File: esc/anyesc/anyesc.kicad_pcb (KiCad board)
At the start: 4 copper layers, 42.2 x 17.8 mm, 46 parts, among them J1 USB_C_Receptacle_USB2.0, J2 Conn_01x04, J3 5530843-7, SW1 SW_Push, SW2 SW_Push, U1 RP2040, U2 W25Q64JVXGIQ, U3 B-G431B-ESC1, Y1 12MHz

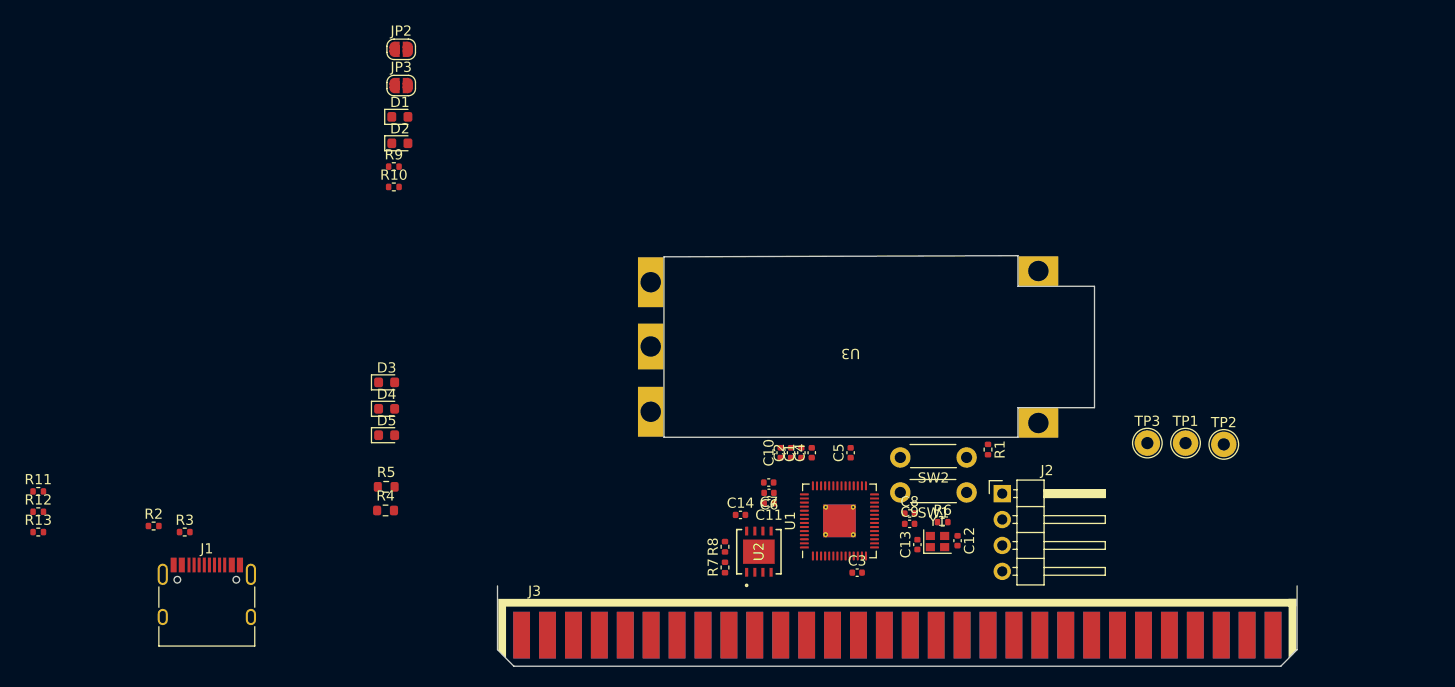
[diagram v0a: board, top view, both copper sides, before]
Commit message: Feat[anyesc]: initial anyesc pcb design
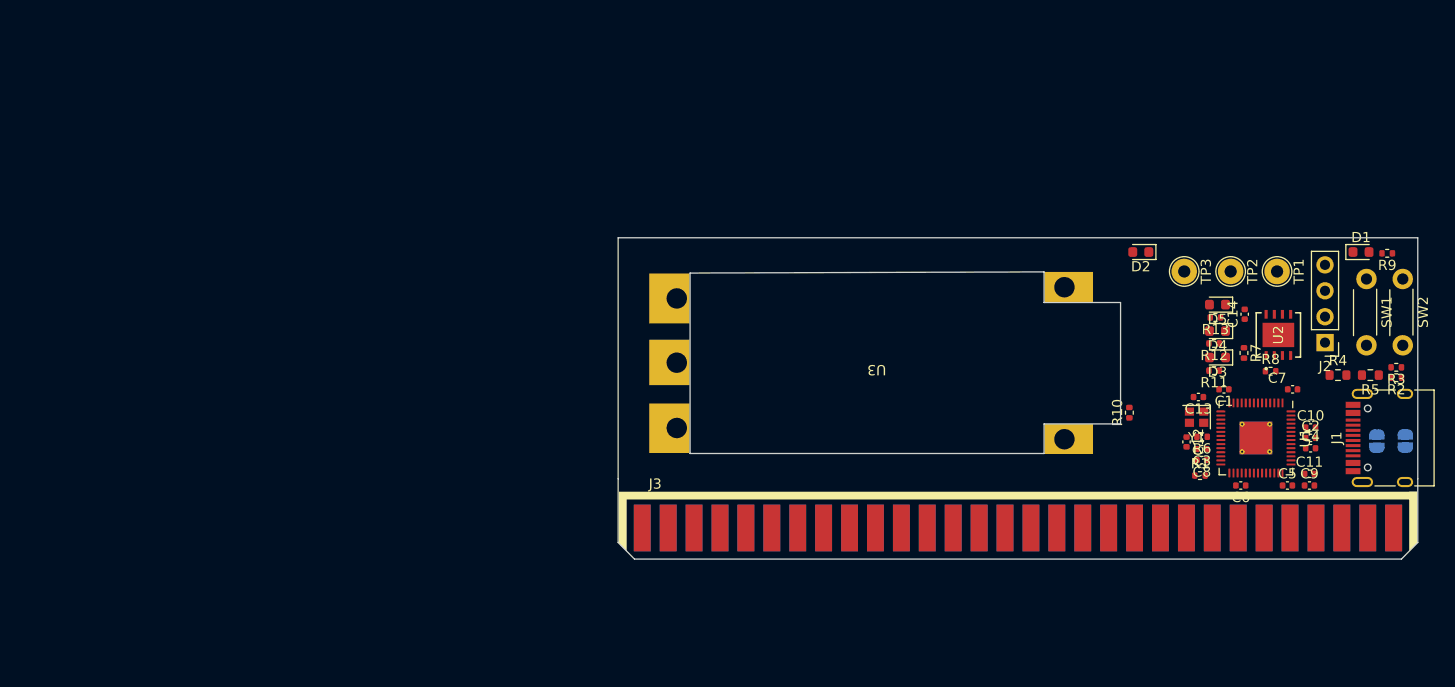
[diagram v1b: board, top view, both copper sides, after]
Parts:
- J2: footprint Connector_PinHeader_2.54mm:PinHeader_1x04_P2.54mm_Horizontal -> Connector_PinHeader_2.54mm:PinHeader_1x04_P2.54mm_Vertical
- JP2, JP3: moved to B.Cu
- moved R2 122.7 mm to (184.0, 105.2), turned to 180 degrees
- moved R3 119.9 mm to (184.0, 104.2), turned to 180 degrees
- moved J1 117.6 mm to (183.8, 111.1), turned to 90 degrees
- moved R13 117.3 mm to (166.3, 99.3), turned to 180 degrees
- moved R12 116.4 mm to (166.2, 101.9), turned to 180 degrees
- moved R11 115.9 mm to (166.2, 104.5), turned to 180 degrees
- moved JP3 104.4 mm to (184.9, 111.4), turned to -90 degrees
- moved JP2 103.1 mm to (182.1, 111.4), turned to -90 degrees
- moved R9 97.7 mm to (183.2, 93.0), turned to 180 degrees
- moved R5 97.1 mm to (181.5, 105.0), turned to 180 degrees
- moved D1 95.1 mm to (180.6, 92.9)
- moved R4 94.3 mm to (178.3, 105.0)
- moved D5 82.4 mm to (166.5, 98.1), turned to 180 degrees
- moved D4 81.8 mm to (166.5, 100.7), turned to 180 degrees
- moved D3 81.5 mm to (166.5, 103.2), turned to 180 degrees
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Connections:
- J3 pad 19: +3V3 -> +12V
- J3 pad 20: +3V3 -> +12V
- J3 pad 21: /BOARD_TX -> +12V
- J3 pad 22: /BOARD_RX -> +12V
- J3 pad 23: /BOARD_TX_1 -> +12V
- J3 pad 24: /BOARD_RX_1 -> +12V
- J3 pad 25: GND -> +12V
- J3 pad 26: GND -> +12V
- J3 pad 27: GND -> +12V
- J3 pad 28: GND -> +12V
- J3 pad 29: GND -> +12V
- J3 pad 30: GND -> +12V
- J3 pad 31: GND -> +12V
- J3 pad 32: GND -> +12V
- J3 pad 33: GND -> +12V
- J3 pad 34: GND -> +12V
- J3 pad 35: GND -> +12V
- J3 pad 36: GND -> +12V
- J3 pad 43: +12V -> GND
- J3 pad 44: +12V -> GND
- J3 pad 45: +12V -> GND
- J3 pad 46: +12V -> GND
- J3 pad 47: +12V -> GND
- J3 pad 48: +12V -> GND
- J3 pad 49: +12V -> GND
- J3 pad 50: +12V -> GND
- J3 pad 51: +12V -> GND
- J3 pad 52: +12V -> GND
- J3 pad 53: +12V -> GND
- J3 pad 54: +12V -> GND
- J3 pad 55: +12V -> +3V3
- J3 pad 56: +12V -> +3V3
- J3 pad 57: +12V -> /BOARD_TX
- J3 pad 58: +12V -> /BOARD_RX
- J3 pad 59: +12V -> /BOARD_TX_1
- J3 pad 60: +12V -> /BOARD_RX_1
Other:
- board size 42.2 x 17.8 mm -> 78.4 x 23.6 mm

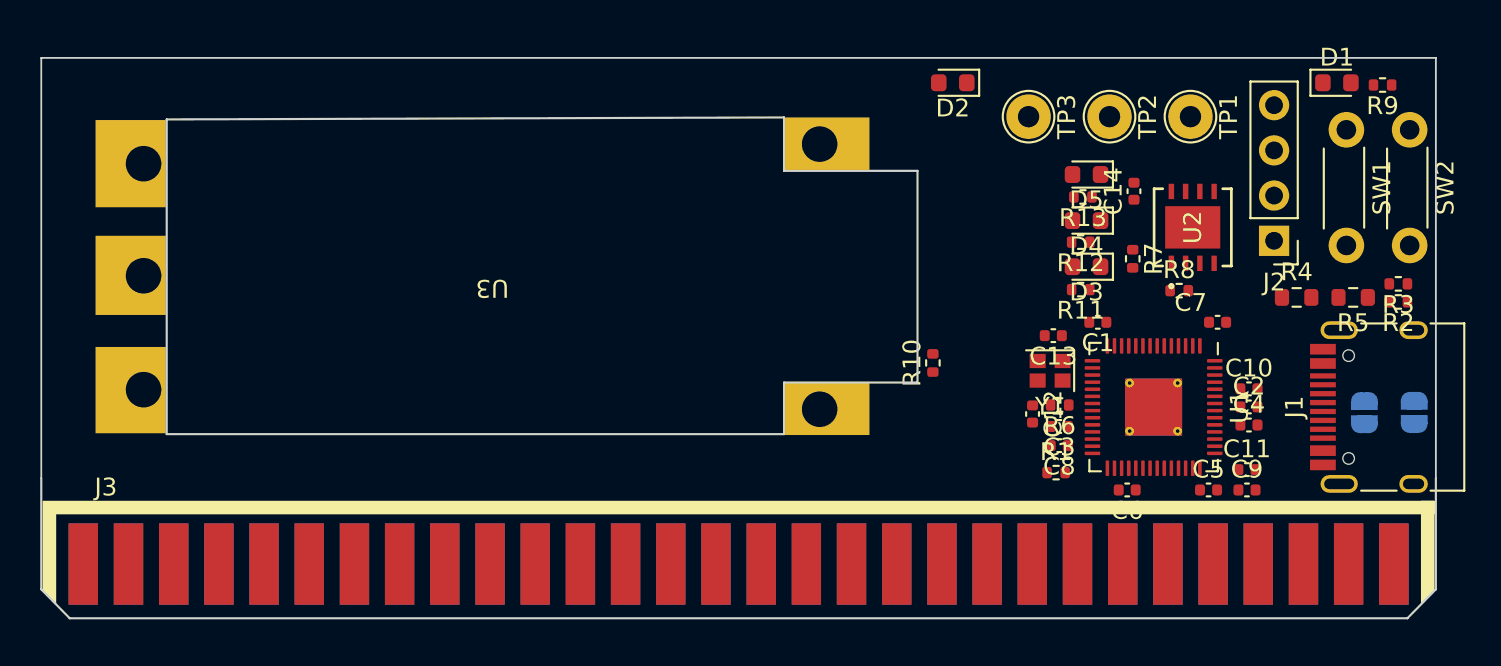
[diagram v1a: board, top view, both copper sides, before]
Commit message: Feat[anyesc]: routing complete with concerningly tight phase routing
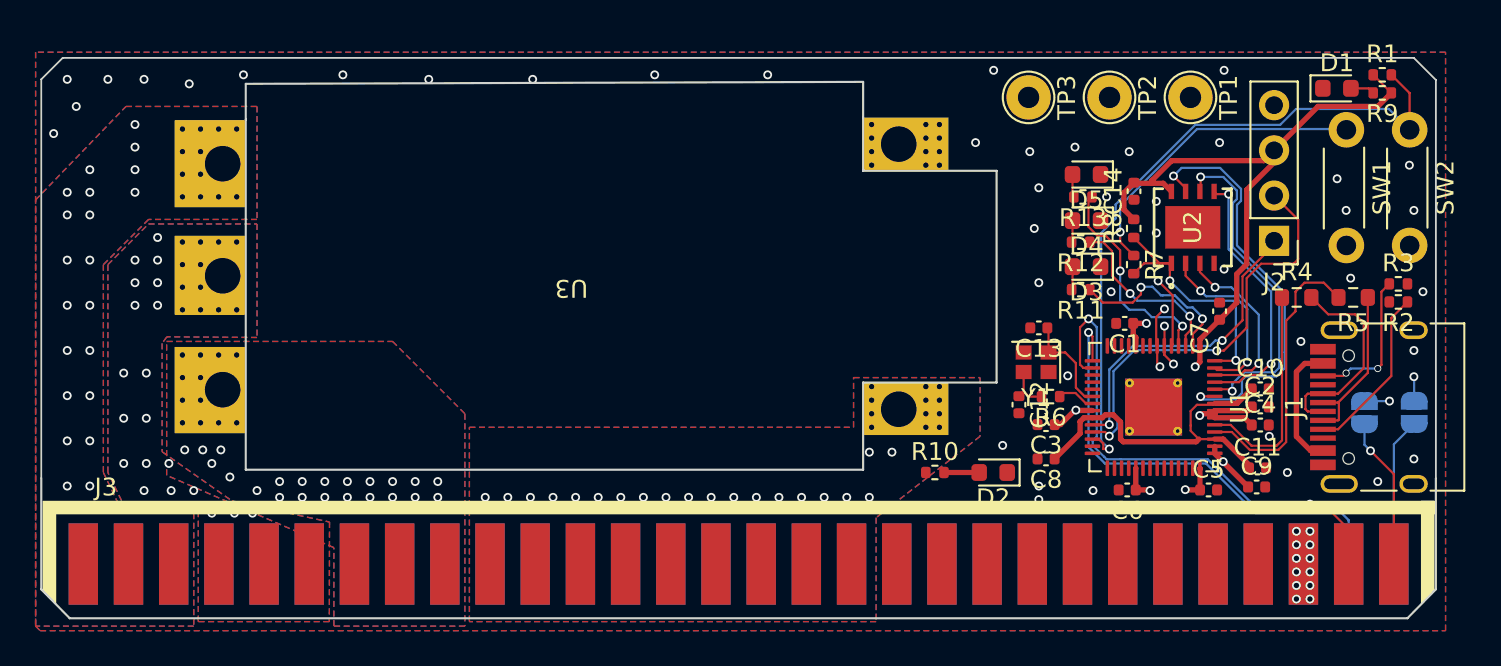
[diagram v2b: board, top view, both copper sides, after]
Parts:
- moved R1 28.9 mm to (183.1, 92.5)
- moved D2 22.0 mm to (161.3, 114.8)
- moved R10 6.16 mm to (158.0, 114.8), turned to 0 degrees
- moved U3 4.45 mm to (137.6, 104.0)
- moved R8 4.33 mm to (169.2, 101.1), turned to 90 degrees
- moved C1 1.51 mm to (168.7, 106.4)
- moved TP1 1.08 mm to (172.4, 93.7)
- moved TP2 1.08 mm to (167.8, 93.7)
- moved TP3 1.08 mm to (163.3, 93.7)
- moved C8 1.05 mm to (164.2, 114.0)
- moved C12 0.93 mm to (162.7, 111.0)
- moved C13 0.92 mm to (163.8, 106.7)
- moved Y1 0.92 mm to (163.7, 108.6)
- moved C3 0.75 mm to (164.2, 112.1)
- moved R6 0.70 mm to (164.5, 110.5)
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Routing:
- net +3V3: track 0.00 -> 53.3 mm, vias 0 -> 20
- net /RP2040/RUN: track 0.00 -> 38.4 mm, vias 0 -> 1
- net /UART1_RX: track 0.00 -> 34.0 mm, vias 0 -> 3
- net /UART1_TX: track 0.00 -> 31.9 mm, vias 0 -> 3
- net /BOARD_RX: track 0.00 -> 29.2 mm, vias 0 -> 2
- net /BOARD_TX: track 0.00 -> 26.9 mm, vias 0 -> 1
- net /RP2040/SWDIO: track 0.00 -> 23.8 mm, vias 0 -> 2
- net /RP2040/QSPI_SD3: track 0.00 -> 23.6 mm, vias 0 -> 2
- net /ESC_PWM: track 0.00 -> 22.1 mm, vias 0 -> 1
- net /RP2040/+1.1V: track 0.00 -> 20.1 mm
- net /RP2040/QSPI_SCK: track 0.00 -> 18.8 mm, vias 0 -> 2
- net /RP2040/SWCLK: track 0.00 -> 17.9 mm, vias 0 -> 2
- net /RP2040/USB_BOOT: track 0.00 -> 17.6 mm, vias 0 -> 1
- net Net-(U1-USB_DM): track 0.00 -> 16.2 mm
- net /RP2040/QSPI_SD0: track 0.00 -> 15.0 mm, vias 0 -> 2
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- added copper zone on B.Cu, net +12V
- added copper zone on F.Cu, net +12V
- added copper zone on In1.Cu, net +12V
- added copper zone on In2.Cu, net +12V
- added copper zone on In2.Cu, net +3V3
- added copper zone on B.Cu, net /PHASE_A
- added copper zone on F.Cu, net /PHASE_A
- added copper zone on In1.Cu, net /PHASE_A
- added copper zone on In2.Cu, net /PHASE_A
- added copper zone on B.Cu, net /PHASE_B
- added copper zone on F.Cu, net /PHASE_B
- added copper zone on In1.Cu, net /PHASE_B
- added copper zone on In2.Cu, net /PHASE_B
- added copper zone on B.Cu, net /PHASE_C
- added copper zone on F.Cu, net /PHASE_C
- added copper zone on In1.Cu, net /PHASE_C
- added copper zone on In2.Cu, net /PHASE_C
- added copper zone on B.Cu, net GND
- added copper zone on F.Cu, net GND
- added copper zone on In1.Cu, net GND
- added copper zone on In2.Cu, net GND
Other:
- outline, holes or cut-outs redrawn
